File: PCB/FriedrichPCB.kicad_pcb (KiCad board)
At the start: 2 copper layers, 246.7 x 94.2 mm, 122 parts, among them U1 ATmega32U4-AU, U2 SRV05-4, X1 Crystal_GND24_Small

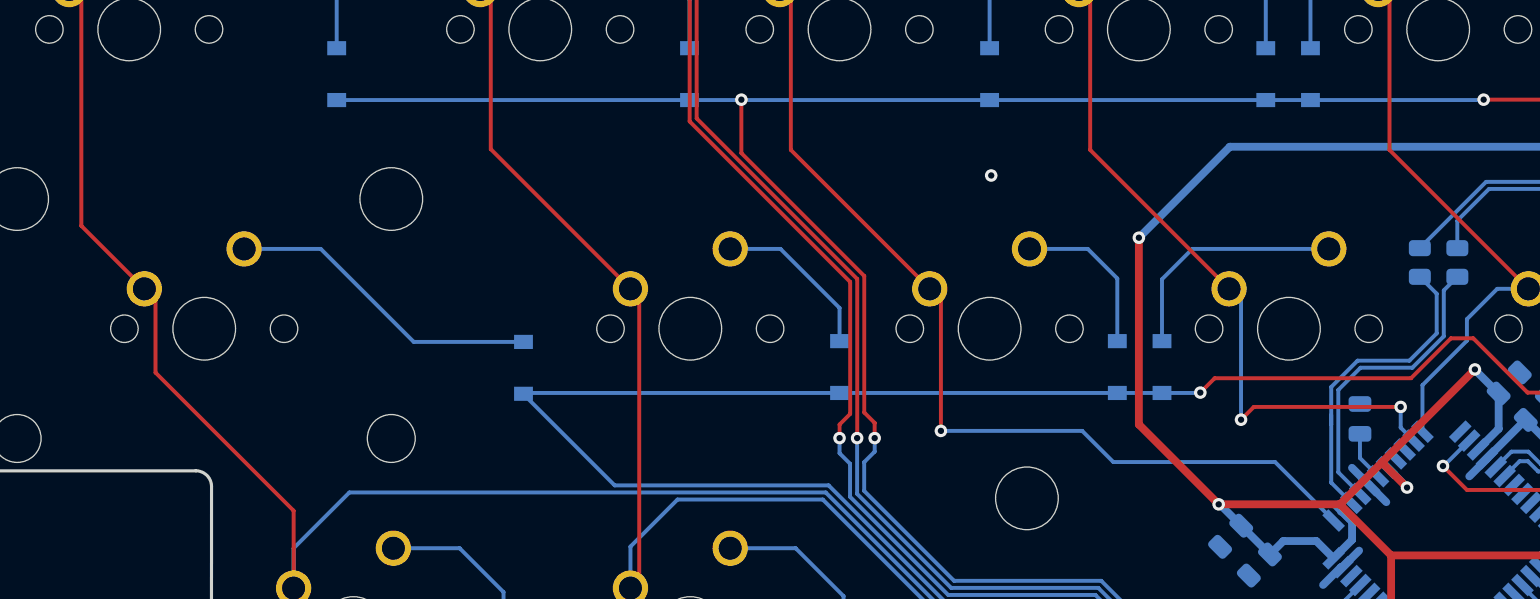
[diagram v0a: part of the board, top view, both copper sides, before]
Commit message: add Capslock LED
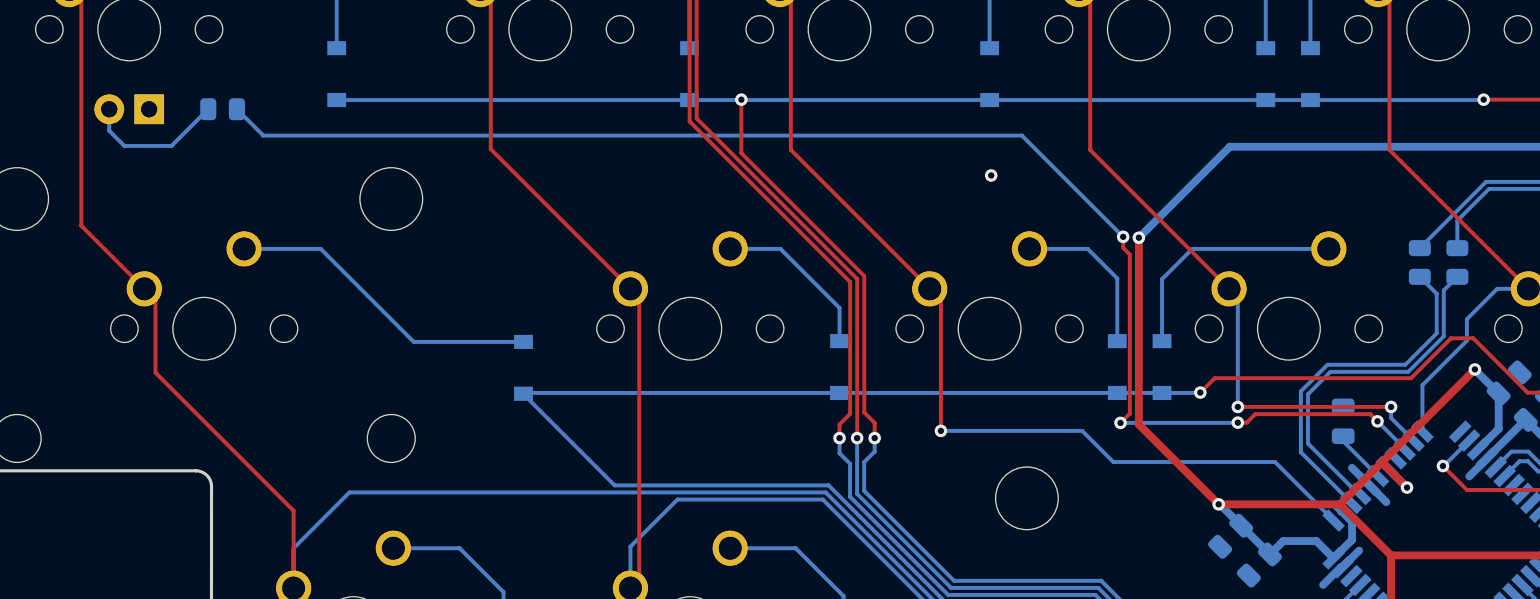
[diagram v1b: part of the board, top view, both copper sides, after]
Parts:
- removed MX27: MX-NoLED, MX_Only:MXOnly-1.75U-NoLED
- added MX26: MX-LED, MX_Only:MXOnly-1.75U, F.Cu at (41.6, 94.8)
- added R6: 1k, Resistor_SMD:R_0805_2012Metric, B.Cu at (47.5, 99.9)
- moved C7 1.08 mm to (118.8, 119.7)
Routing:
- net Net-(R6-Pad2): track 0.00 -> 91.3 mm, vias 0 -> 4
- net LED: track 0.00 -> 9.04 mm
- net Net-(R1-Pad2): track 19.5 -> 22.1 mm
- net Net-(R2-Pad2): track 20.7 -> 22.6 mm
- net col3: track 88.6 -> 87.4 mm
